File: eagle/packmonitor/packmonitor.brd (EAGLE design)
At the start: 62.3 x 18 mm, 35 parts, among them IC1 24C64, IC2 TCA4311A, IC3 AP2411, IC4 ACS712, Q1 PCHAN

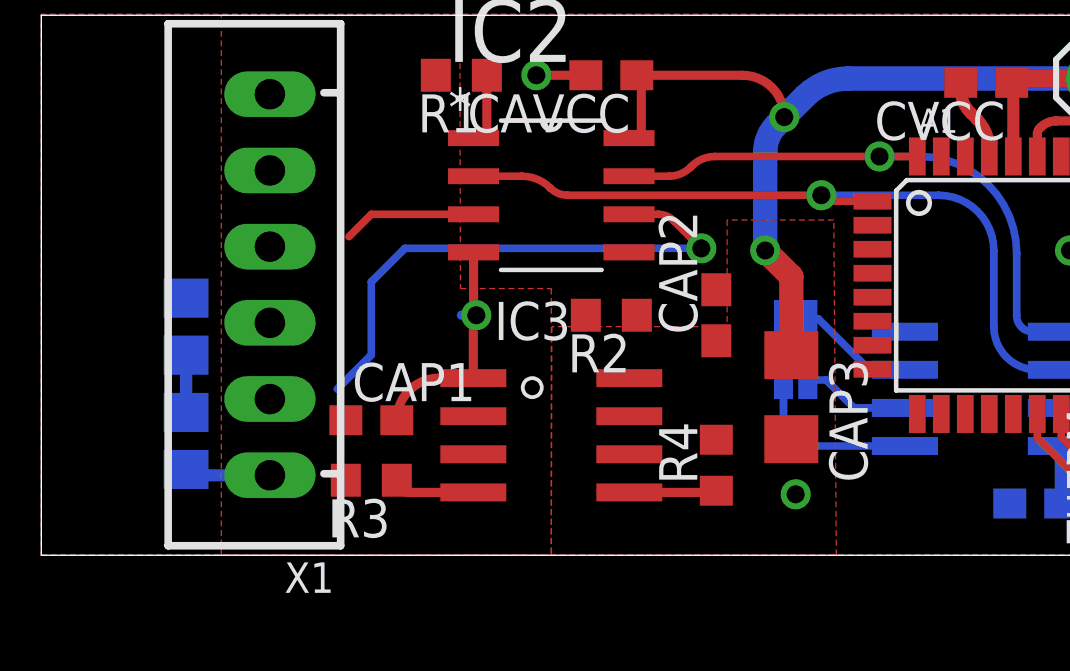
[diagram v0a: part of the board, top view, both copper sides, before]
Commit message: got rid of input power switch
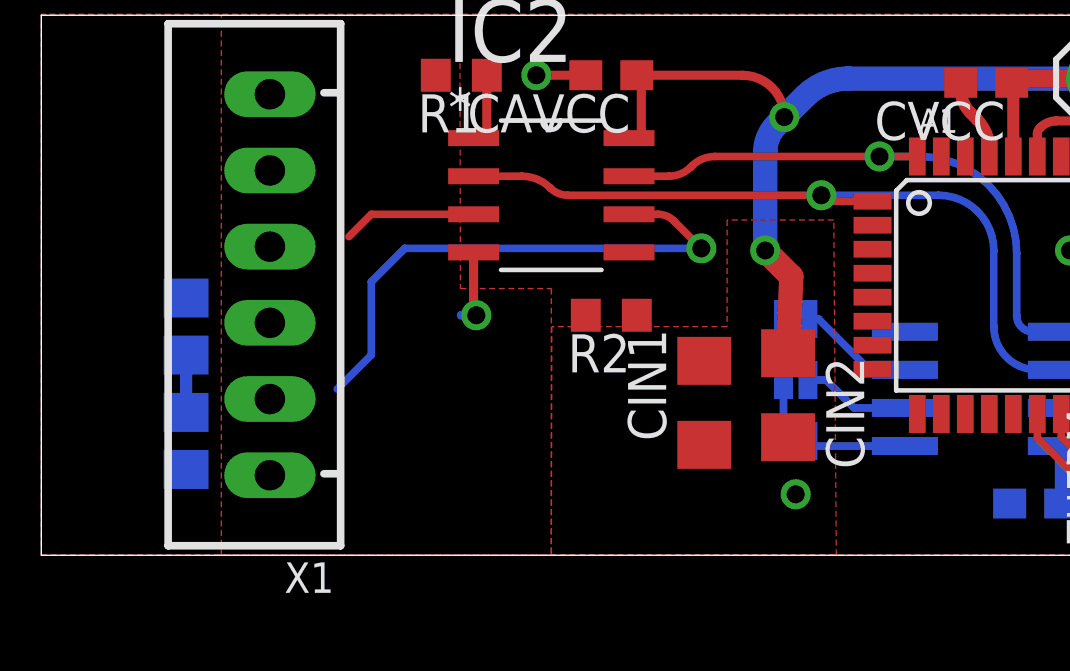
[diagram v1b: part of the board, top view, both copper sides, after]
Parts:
- removed CAP1, CAP2: 100n, rcl:C0603
- removed CAP3: 120u, rcl:C1206
- removed IC3: AP2411, ti-special:SO08
- removed R3, R4: 10K, rcl:R0603
- added CIN1, CIN2: 120u, rcl:C1206
- R2: value (none) -> 10K
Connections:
- removed net ENBUSPWR: IC3.4, R3.1
- removed net PWRFAULT: IC3.5, R4.1
- removed net VCCIO: CAP1.1, IC3.2, IC3.3, R1.2, R3.2, RBUS1.2, X1.1
- net GND: now also CIN1.2, CIN2.2; no longer CAP1.2, CAP2.2, CAP3.2, IC3.1
- net VCC: now also CIN1.1, CIN2.1, R1.2, RBUS1.2, X1.1; no longer CAP2.1, CAP3.1, IC3.6, IC3.7, IC3.8, R4.2
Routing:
- net GND: track 14.3 -> 9.04 mm
- net PWRFAULT: track 2.92 -> 0.00 mm
- net VCCIO: track 2.85 -> 0.00 mm
- net ENBUSPWR: track 2.72 -> 0.00 mm
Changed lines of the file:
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@@
 </element>
 <element name="R1" library="rcl" package="R0603" value="10K" x="14" y="16" rot="R180"/>
-<element name="R2" library="rcl" package="R0603" value="" x="19" y="8" rot="R180"/>
-<element name="IC3" library="ti-special" package="SO08" value="AP2411" x="17" y="4" rot="R270"/>
+<element name="R2" library="rcl" package="R0603" value="10K" x="19" y="8" rot="R180"/>
 <element name="CTCA" library="rcl" package="C0603" value="100n" x="38.606" y="8.124" rot="R90"/>
-<element name="R3" library="rcl" package="R0603" value="10K" x="11" y="2.5" rot="R180"/>
-<element name="R4" library="rcl" package="R0603" value="10K" x="22.5" y="3" rot="R90"/>
-<element name="CAP1" library="rcl" package="C0603" value="100n" x="11" y="4.5"/>
-<element name="CAP2" library="rcl" package="C0603" value="100n" x="22.5" y="8" rot="R90"/>
-<element name="CAP3" library="rcl" package="C1206" value="120u" x="25" y="5.27" rot="R270"/>
+<element name="CIN2" library="rcl" package="C1206" value="120u" x="24.892" y="5.334" rot="R270"/>
 <element name="TR1" library="rcl" package="R0805" value="50K" x="39.37" y="5.08" rot="MR180"/>
 <element name="TR2" library="rcl" package="R0805" value="50K" x="44.45" y="5.08" rot="MR180"/>
@@
 <element name="RGATE" library="rcl" package="R0603" value="470R" x="38.862" y="13.462" rot="R180"/>
 <element name="CACS" library="rcl" package="C0603" value="100n" x="53.34" y="7.62" rot="R270"/>
+<element name="CIN1" library="rcl" package="C1206" value="120u" x="22.098" y="5.08" rot="R90"/>
 </elements>
 <signals>
@@
 <contactref element="CEEP" pad="1"/>
 <contactref element="R2" pad="2"/>
-<contactref element="IC3" pad="6"/>
-<contactref element="IC3" pad="7"/>
-<contactref element="IC3" pad="8"/>
 <contactref element="IC2" pad="8"/>
 <contactref element="CTCA" pad="1"/>
-<contactref element="R4" pad="2"/>
-<contactref element="CAP2" pad="1"/>
-<contactref element="CAP3" pad="1"/>
+<contactref element="CIN2" pad="1"/>
 <polygon width="0.3048" layer="1" spacing="0.3048" isolate="0.3048" rank="4">
 <vertex x="17.018" y="7.62"/>
@@
 <via x="24.13" y="10.16" extent="1-16" drill="0.6"/>
 <wire x1="24.13" y1="10.16" x2="25" y2="9.29" width="0.8128" layer="1"/>
-<wire x1="25" y1="9.29" x2="25" y2="6.67" width="0.8128" layer="1"/>
+<wire x1="25" y1="9.29" x2="24.892" y2="6.734" width="0.8128" layer="1"/>
 <wire x1="19.85" y1="16" x2="23.37" y2="16" width="0.3048" layer="1"/>
 <wire x1="23.37" y1="16" x2="24.765" y2="14.605" width="0.3048" layer="1" curve="-90"/>
@@
 <wire x1="36.576" y1="8.86485" x2="36.576" y2="4.064" width="0.8128" layer="16"/>
 <wire x1="36.576" y1="4.064" x2="38.1" y2="2.54" width="0.8128" layer="16"/>
+<contactref element="CIN1" pad="1"/>
+<contactref element="X1" pad="1"/>
+<contactref element="R1" pad="2"/>
+<contactref element="RBUS1" pad="2"/>
 <wire x1="36.576" y1="8.86485" x2="36.2926" y2="7" width="0" layer="19" extent="1-16"/>
-<wire x1="24.7396" y1="5.842" x2="25" y2="6.67" width="0" layer="19" extent="1-16"/>
+<wire x1="24.7396" y1="5.842" x2="24.892" y2="6.734" width="0" layer="19" extent="1-16"/>
+<wire x1="25.146" y1="2.032" x2="24.7396" y2="3.81" width="0" layer="19" extent="16-16"/>
+<wire x1="18.15" y1="8" x2="19.5908" y2="13.905" width="0" layer="19" extent="1-1"/>
+<wire x1="13.15" y1="16" x2="19.85" y2="16" width="0" layer="19" extent="1-1"/>
+<wire x1="7.62" y1="2.667" x2="18.15" y2="8" width="0" layer="19" extent="1-1"/>
+<wire x1="4.826" y1="2.86" x2="7.62" y2="2.667" width="0" layer="19" extent="16-16"/>
+<wire x1="22.098" y1="3.68" x2="4.826" y2="2.86" width="0" layer="19" extent="1-16"/>
 </signal>
 <signal name="GND">
@@
 <contactref element="GROUND" pad="2"/>
 <contactref element="IC2" pad="4"/>
-<contactref element="IC3" pad="1"/>
 <contactref element="CTCA" pad="2"/>
-<contactref element="CAP1" pad="2"/>
-<contactref element="CAP2" pad="2"/>
-<contactref element="CAP3" pad="2"/>
-<wire x1="11.85" y1="4.5" x2="13.255" y2="5.905" width="0.3048" layer="1" curve="-90"/>
-<wire x1="13.255" y1="5.905" x2="14.4" y2="5.905" width="0.3048" layer="1"/>
+<contactref element="CIN2" pad="2"/>
 <polygon width="0.3048" layer="16" spacing="0.254" isolate="0.254" rank="5">
 <vertex x="0" y="18"/>
@@
 <wire x1="14.4092" y1="10.095" x2="14.4092" y2="8" width="0.3048" layer="1"/>
 <wire x1="14.4092" y1="8" x2="14.5" y2="8" width="0.3048" layer="1"/>
-<wire x1="14.4" y1="5.905" x2="14.4" y2="8" width="0.3048" layer="1"/>
 <wire x1="14.4" y1="8" x2="14.5" y2="8" width="0.3048" layer="1"/>
 <via x="16.5" y="16" extent="1-16" drill="0.6"/>
@@
 <wire x1="46.482" y1="6.858" x2="47.7012" y2="6.858" width="0.3048" layer="1"/>
 <wire x1="47.7012" y1="6.858" x2="47.625" y2="7.5438" width="0.3048" layer="1"/>
-<wire x1="28.786" y1="7.451" x2="25" y2="3.87" width="0" layer="19" extent="1-16"/>
-<wire x1="36.2926" y1="7.8" x2="33.986" y2="4.911" width="0" layer="19" extent="1-16"/>
+<contactref element="CIN1" pad="2"/>
+<wire x1="58.42" y1="4.628" x2="58.42" y2="8.128" width="0" layer="19" extent="1-1"/>
+<wire x1="55.626" y1="2.098" x2="58.42" y2="4.628" width="0" layer="19" extent="16-16"/>
+<wire x1="53.086" y1="2.286" x2="55.626" y2="2.098" width="0" layer="19" extent="16-16"/>
+<wire x1="52.07" y1="5.334" x2="53.086" y2="2.286" width="0" layer="19" extent="1-1"/>
+<wire x1="53.34" y1="6.77" x2="52.07" y2="5.334" width="0" layer="19" extent="1-1"/>
+<wire x1="48.326" y1="5.08" x2="52.07" y2="5.334" width="0" layer="19" extent="16-16"/>
+<wire x1="47.7012" y1="6.858" x2="48.326" y2="5.08" width="0" layer="19" extent="1-16"/>
+<wire x1="46.99" y1="3.556" x2="48.326" y2="5.08" width="0" layer="19" extent="16-16"/>
+<wire x1="43.5" y1="5.08" x2="46.482" y2="6.858" width="0" layer="19" extent="16-16"/>
+<wire x1="41.91" y1="3.556" x2="43.5" y2="5.08" width="0" layer="19" extent="16-16"/>
+<wire x1="38.42" y1="5.08" x2="41.91" y2="3.556" width="0" layer="19" extent="16-16"/>
+<wire x1="36.2926" y1="7.8" x2="38.42" y2="5.08" width="0" layer="19" extent="1-16"/>
+<wire x1="38.606" y1="8.974" x2="36.2926" y2="7.8" width="0" layer="19" extent="1-1"/>
+<wire x1="33.986" y1="4.911" x2="36.2926" y2="7.8" width="0" layer="19" extent="1-16"/>
+<wire x1="32.28" y1="1.724" x2="33.986" y2="4.911" width="0" layer="19" extent="16-16"/>
+<wire x1="28.786" y1="7.451" x2="33.986" y2="4.911" width="0" layer="19" extent="16-16"/>
+<wire x1="24.892" y1="3.934" x2="28.786" y2="7.451" width="0" layer="19" extent="1-16"/>
+<wire x1="31.6" y1="13.2926" x2="28.786" y2="7.451" width="0" layer="19" extent="1-16"/>
+<wire x1="40.176" y1="15.89" x2="38.606" y2="8.974" width="0" layer="19" extent="1-1"/>
+<wire x1="14.5" y1="8" x2="24.892" y2="3.934" width="0" layer="19" extent="1-16"/>
+<wire x1="16.5" y1="16" x2="14.4092" y2="10.095" width="0" layer="19" extent="1-1"/>
+<wire x1="7.62" y1="10.287" x2="14" y2="8" width="0" layer="19" extent="16-16"/>
+<wire x1="4.826" y1="8.57" x2="7.62" y2="10.287" width="0" layer="19" extent="16-16"/>
+<wire x1="7.62" y1="5.207" x2="4.826" y2="8.57" width="0" layer="19" extent="16-16"/>
+<wire x1="7.62" y1="15.367" x2="7.62" y2="10.287" width="0" layer="19" extent="1-1"/>
+<wire x1="22.098" y1="6.48" x2="7.62" y2="5.207" width="0" layer="19" extent="1-1"/>
 </signal>
 <signal name="A0">
@@
 </signal>
 <signal name="VCCIO">
-<contactref element="R1" pad="2"/>
-<contactref element="IC3" pad="3"/>
-<contactref element="IC3" pad="2"/>
 <polygon width="0.3048" layer="1" spacing="0.3048" isolate="0.3048" rank="5">
 <vertex x="6" y="18"/>
@@
 <vertex x="6" y="0"/>
 </polygon>
-<contactref element="R3" pad="2"/>
-<contactref element="CAP1" pad="1"/>
-<contactref element="X1" pad="1"/>
-<contactref element="RBUS1" pad="2"/>
-<wire x1="4.826" y1="2.86" x2="5.119" y2="2.667" width="0.4064" layer="16"/>
-<wire x1="5.119" y1="2.667" x2="7.62" y2="2.667" width="0.4064" layer="16"/>
 </signal>
 <signal name="N$6">
@@
 <wire x1="19.85" y1="8" x2="19.5908" y2="10.095" width="0" layer="19" extent="1-1"/>
 </signal>
-<signal name="ENBUSPWR">
-<contactref element="IC3" pad="4"/>
-<contactref element="R3" pad="1"/>
-<wire x1="11.85" y1="2.5" x2="12.255" y2="2.095" width="0.3048" layer="1" curve="90"/>
-<wire x1="12.255" y1="2.095" x2="14.4" y2="2.095" width="0.3048" layer="1"/>
-</signal>
-<signal name="PWRFAULT">
-<contactref element="IC3" pad="5"/>
-<contactref element="R4" pad="1"/>
-<wire x1="19.6" y1="2.095" x2="22.445" y2="2.095" width="0.3048" layer="1"/>
-<wire x1="22.445" y1="2.095" x2="22.5" y2="2.15" width="0.3048" layer="1" curve="90"/>
-</signal>
 <signal name="VBUS">

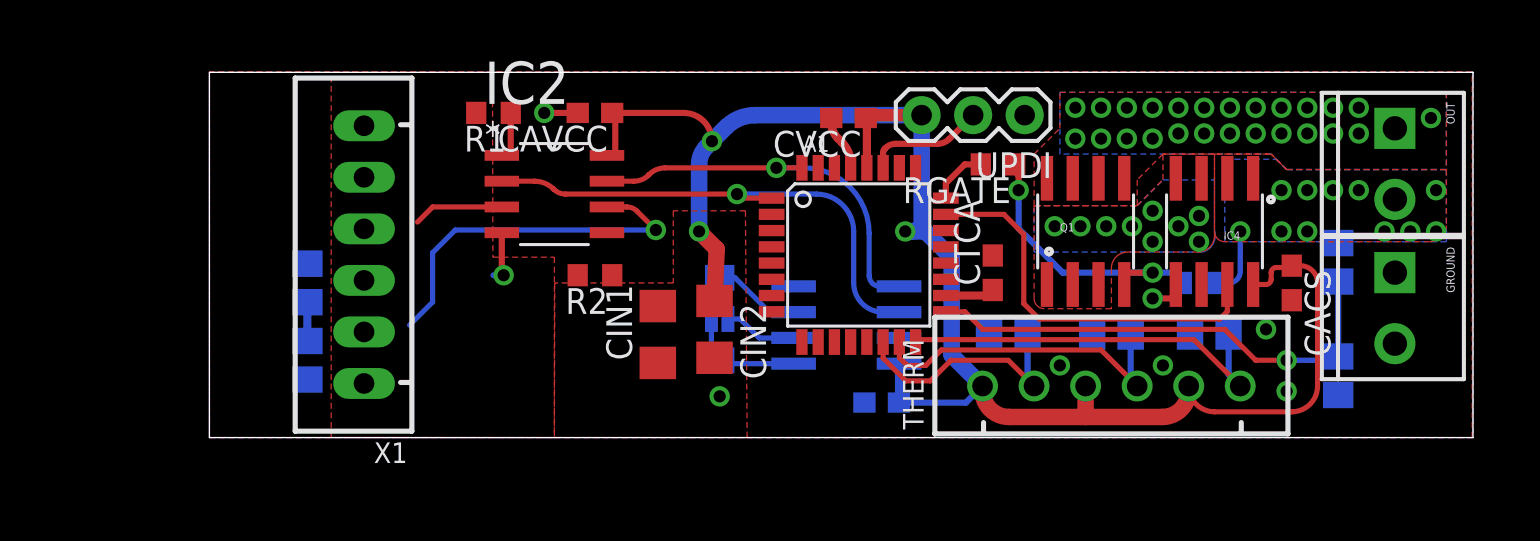
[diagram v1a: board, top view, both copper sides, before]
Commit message: switched to avr128da32 chip & low side disconnect
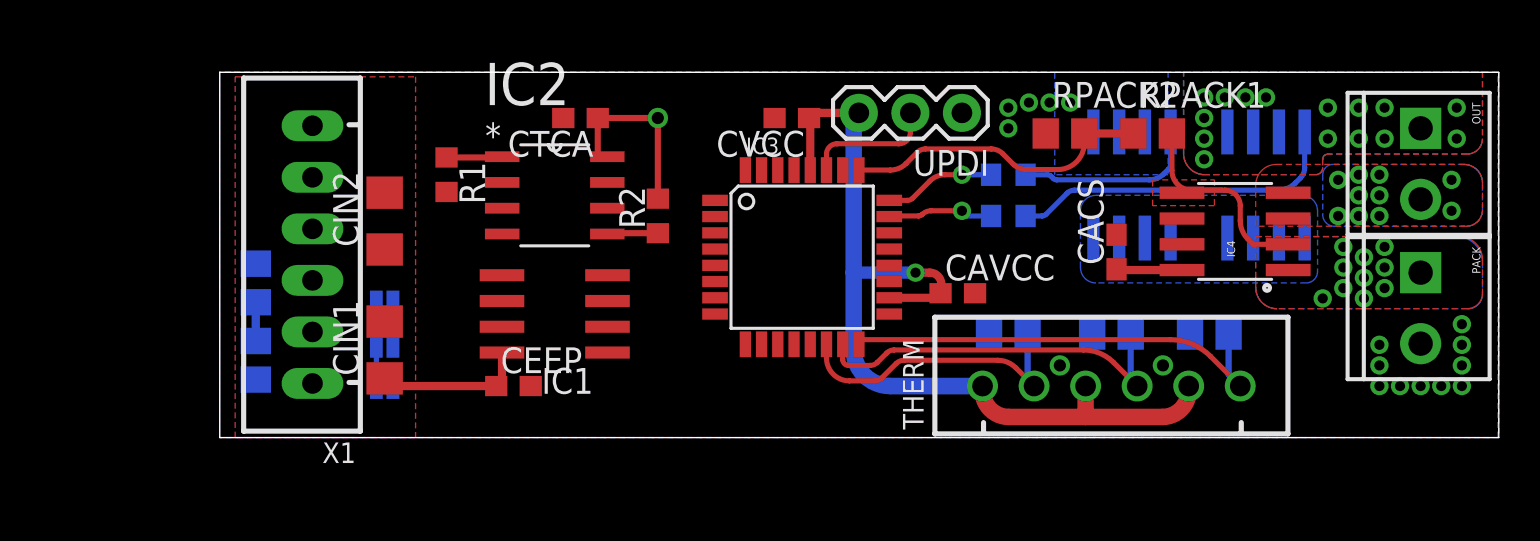
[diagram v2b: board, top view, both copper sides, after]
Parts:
- removed A1: ATMEGA4808, microchip-special:TQFP32-08
- removed GROUND: (no value), SparkFun-Connectors:SCREWTERMINAL-3.5MM-2
- removed Q1: PCHAN, SparkFun-DiscreteSemi:SO08
- removed RG-PU: 10K, rcl:R0603
- removed RGATE: 470R, rcl:R0603
- added IC3: AVRXDA32TQFP, microchip-special:TQFP32-08
- added PACK: (no value), SparkFun-Connectors:SCREWTERMINAL-3.5MM-2
- added QCHG, QDIS: NFET, SparkFun-DiscreteSemi:SO08
- added RGATE1, RGATE2: 470R, rcl:R0603
- CIN2: value 120u -> DNP 120u
- moved CTCA 21.7 mm to (18.3, 15.7), turned to 180 degrees
- moved CAVCC 20.0 mm to (36.9, 7.11), turned to 0 degrees
- moved CEEP 18.2 mm to (15.0, 2.54), flipped to the top
- moved RPACK2 18.0 mm to (42.2, 15.0), flipped to the top, turned to 0 degrees
- moved CIN2 17.1 mm to (8.64, 10.7), turned to 90 degrees
- moved JP1 16.6 mm to (8.64, 2.54)
- moved JP2 16.6 mm to (8.64, 4.57)
- moved JP3 16.6 mm to (8.64, 6.60)
- moved IC1 14.4 mm to (17.0, 6.10), flipped to the top
- moved CIN1 13.5 mm to (8.64, 4.32)
- moved RPACK1 11.1 mm to (46.5, 15.0), flipped to the top, turned to 0 degrees
- moved CACS 8.77 mm to (44.7, 9.14), turned to 90 degrees
- moved R2 4.26 mm to (22.1, 10.9), turned to 90 degrees
- moved R1 3.83 mm to (11.7, 13.0), turned to 270 degrees
- moved UPDI 3.09 mm to (37.1, 16.0)
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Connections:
- net N$6 renamed BUSENABLE
- removed net GATE: Q1.4, RG-PU.1, RGATE.1
- removed net GATEDRV: A1.24, RGATE.2
- removed net P+IN: IC4.3, IC4.4, Q1.1, Q1.2, Q1.3
- removed net P+OUT: OUT.1, Q1.5, Q1.6, Q1.7, Q1.8
- removed net SCL: A1.1, IC1.6, IC2.2
- removed net SDA: A1.32, IC1.5, IC2.7
- removed net VBAT: A1.17, RPACK1.1, RPACK2.2
- new net GATECHG: IC3.24, RGATE1.2
- new net GATEDIS: IC3.23, RGATE2.2
- new net N$1: QCHG.4, RGATE1.1
- new net N$2: QDIS.4, RGATE2.1
- new net PACK+: IC4.1, IC4.2, PACK.1, RPACK1.2
- new net PACKOUT+: IC4.3, IC4.4, OUT.2
- new net PACKOUT-: OUT.1, QDIS.1, QDIS.2, QDIS.3
- new net PDISC: QCHG.5, QCHG.6, QCHG.7, QCHG.8, QDIS.5, QDIS.6, QDIS.7, QDIS.8
- new net SCL_C: IC2.2, IC3.9
- new net SCL_H: IC1.6, IC3.1
- new net SDA_C: IC2.7, IC3.8
- new net SDA_H: IC1.5, IC3.32
- net GND: now also IC3.19, IC3.29, PACK.2, QCHG.1, QCHG.2, QCHG.3; no longer A1.19, A1.29, GROUND.1, GROUND.2
- net MVAOUT: no longer A1.23
- net TS0: now also IC3.14; no longer A1.14
- net TS1: now also IC3.15; no longer A1.15
- net TS2: now also IC3.16; no longer A1.16
- net UPDI: now also IC3.27; no longer A1.27
- net VBUS: no longer A1.10
- net VCC: now also IC3.18, IC3.28; no longer A1.18, A1.28
- net VPACK: now also IC3.25, RPACK1.1, RPACK2.2; no longer IC4.1, IC4.2, OUT.2, RG-PU.2, RPACK1.2
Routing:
- net SCL: track 25.4 -> 0.00 mm, vias 1 -> 0
- net VBAT: track 24.2 -> 0.00 mm, vias 1 -> 0
- net VCC: track 92.6 -> 69.3 mm, vias 4 -> 2
- net MVAOUT: track 19.5 -> 0.00 mm
- net SDA: track 19.4 -> 0.00 mm, vias 1 -> 0
- net N$3: track 18.3 -> 0.00 mm, vias 1 -> 0
- net N$2: track 0.00 -> 16.5 mm
- net GATE: track 14.3 -> 0.00 mm, vias 2 -> 0
- net VPACK: track 3.39 -> 15.2 mm, vias 11 -> 0
- net PACK+: track 0.00 -> 9.72 mm, vias 0 -> 10
- net N$1: track 0.00 -> 9.13 mm
- net GND: track 9.04 -> 0.00 mm, vias 7 -> 17
- net GATECHG: track 0.00 -> 5.45 mm, vias 0 -> 1
- net GATEDIS: track 0.00 -> 5.19 mm, vias 0 -> 1
- net N$4: track 4.46 -> 0.00 mm
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- added copper zone on layer 1, net PACK+
- added copper zone on layer 16, net PACK+
- added copper zone on layer 1, net PACKOUT+
- added copper zone on layer 16, net PACKOUT+
- added copper zone on layer 1, net PACKOUT-
- added copper zone on layer 16, net PACKOUT-
- added copper zone on layer 16, net PDISC
- removed copper zone on layer 1, net P+IN
- removed copper zone on layer 16, net P+IN
- removed copper zone on layer 1, net P+OUT
- removed copper zone on layer 16, net P+OUT
- removed copper zone on layer 1, net VCCIO
- removed copper zone on layer 1, net VPACK
- removed copper zone on layer 16, net VPACK
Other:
- board size 62.3 x 18 mm -> 63 x 18 mm

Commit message: layout and routing complete, needs fine tuning
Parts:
- removed JP1, JP2: A1, SparkFun-Jumpers:SMT-JUMPER_2_NO_SILK
- removed JP3: A2, SparkFun-Jumpers:SMT-JUMPER_2_NO_SILK
- removed R1, R2: 10K, rcl:R0603
- added RENAPD: 10K, rcl:R0603
- moved CEEP 13.4 mm to (11.4, 15.5), turned to 270 degrees
- moved CTCA 7.98 mm to (19.6, 7.87)
- moved IC2 7.89 mm to (17.5, 4.06)
- moved IC1 7.22 mm to (15.7, 13.2), turned to 0 degrees
- moved CIN1 3.10 mm to (10.4, 1.78), turned to 0 degrees
- moved CACS 2.40 mm to (42.7, 7.87), turned to 180 degrees
- moved CIN2 2.16 mm to (10.2, 12.2), turned to 0 degrees
- moved CAVCC 1.27 mm to (35.6, 7.11)
- moved CVCC 1.27 mm to (27.4, 15.7)
- moved QCHG 1.27 mm to (44.2, 12.4)
- moved QDIS 1.27 mm to (50.8, 12.4)
- moved RPACK2 1.27 mm to (40.9, 15.0)
- moved THERM 1.27 mm to (43.2, 2.54)
- moved TR2 1.27 mm to (43.2, 5.08)
- moved TR3 1.27 mm to (48.0, 5.08)
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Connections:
- net N$3 renamed SDAIN
- net N$4 renamed SCLIN
- removed net A0: IC1.1, JP1.2
- removed net A1: IC1.2, JP2.2
- removed net A2: IC1.3, JP3.2
- net BUSENABLE: now also IC3.12, RENAPD.2; no longer R1.1
- net BUSREADY: now also IC3.11; no longer R2.1
- net GND: now also IC1.1, IC1.2, IC1.3, IC4.6, RENAPD.1; no longer X1.2
- net MVAOUT: now also IC3.21
- net VBUS: now also IC3.10
- net VCC: now also X1.2; no longer JP1.1, JP2.1, JP3.1, R1.2, R2.2
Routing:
- net VCC: track 69.3 -> 111.1 mm, vias 2 -> 3
- net VBUS: track 1.91 -> 31.7 mm, vias 0 -> 1
- net SDAIN: track 0.00 -> 20.0 mm
- net BUSENABLE: track 2.78 -> 18.8 mm, vias 0 -> 2
- net SCL_C: track 0.00 -> 15.9 mm
- net MVAOUT: track 0.00 -> 14.6 mm
- net SCLIN: track 0.00 -> 12.2 mm
- net SCL_H: track 0.00 -> 10.1 mm
- net SDA_H: track 0.00 -> 9.03 mm
- net BUSREADY: track 2.53 -> 9.10 mm, vias 0 -> 2
- net SDA_C: track 0.00 -> 4.23 mm
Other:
- board size 63 x 18 mm -> 61.8 x 18 mm

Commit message: final tweaks, fingers crossed order sent
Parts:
- added CACS1: 1n, rcl:C0603
- renumbered CACS to CACS2, RENAPD to RENA, X1 to HOST_BUS
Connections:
- new net N$3: CACS1.1, IC4.6
- net GND: now also CACS1.2; no longer IC4.6
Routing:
- net N$3: track 0.00 -> 2.38 mm
- net VBUS: track 31.7 -> 31.0 mm
- net PACK+: vias 10 -> 7
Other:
- board text added: "(+)"
- board text added: "(-)"
- board text added: "+"
- board text added: "-"
- board text added: "D"
